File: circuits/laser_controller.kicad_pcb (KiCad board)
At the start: 4 copper layers, 173 x 61.1 mm, 180 parts, among them J1 USB_MINI_B, J2 USB_MINI_B, J5 24V DC IN, J6 CONN_RJ45, Q1 SOT-23, Q2 SOT-23, Q3 SOT-23, Q4 SOT-23, Q5 SOT-23, Q6 SOT-23, SW1 SW_PUSH, SW2 SW_PUSH, SW3 SW_PUSH, U1 SOIC-8_3.9x4.9mm_P1.27mm, U10 QFN-28-1EP_5x5mm_P0.5mm_EP3.3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, U11 SOT-23-5, U12 TSSOP-14_4.4x5mm_P0.65mm, U13 SOT-23, U14 LQFP-64_10x10mm_P0.5mm, U15 TSOT-23-6, U16 TSOT-23-6, U2 SOIC-8_3.9x4.9mm_P1.27mm, U3 SOIC-8_3.9x4.9mm_P1.27mm, U4 SOIC-8_3.9x4.9mm_P1.27mm, U5 SOT-23-5, U6 SOT-23-5, U7 SOT-23-5, U8 SOT-23-5, U9 ESP32-S3-WROOM-1

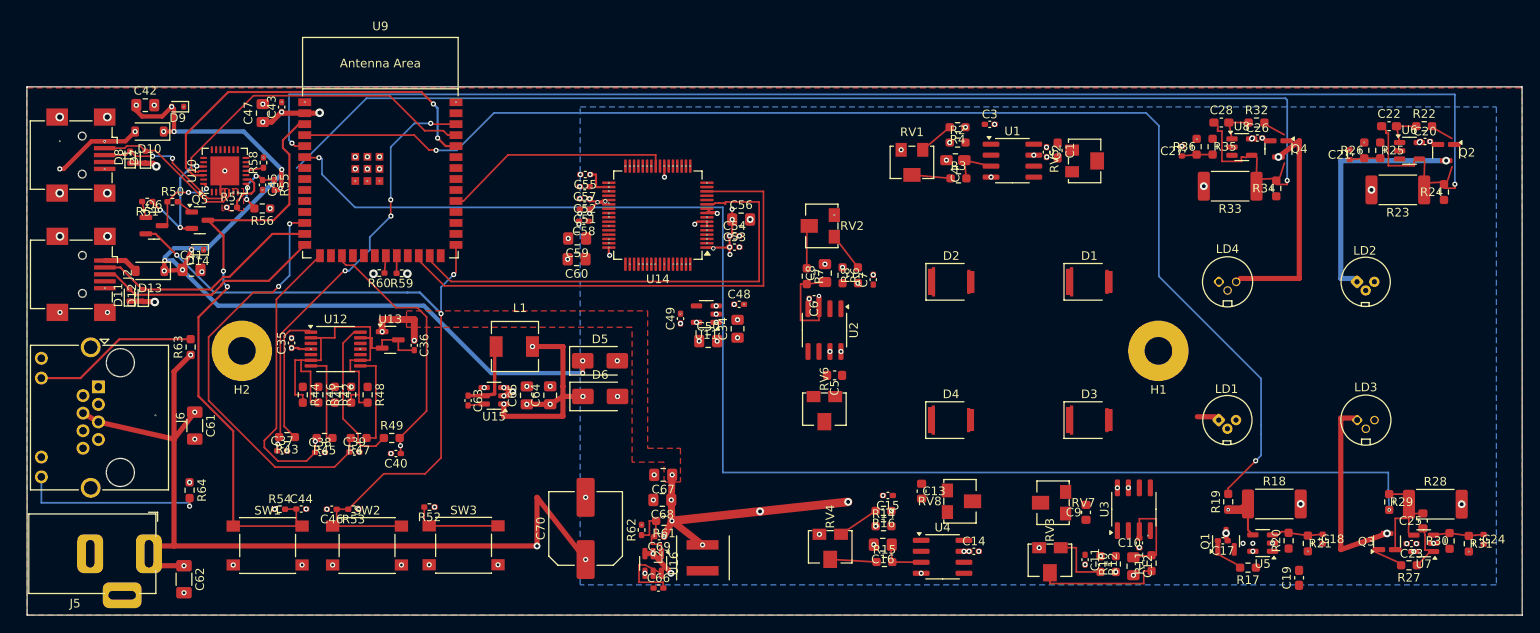
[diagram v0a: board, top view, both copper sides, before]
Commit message: fix(pcb): remove dangling trace stubs
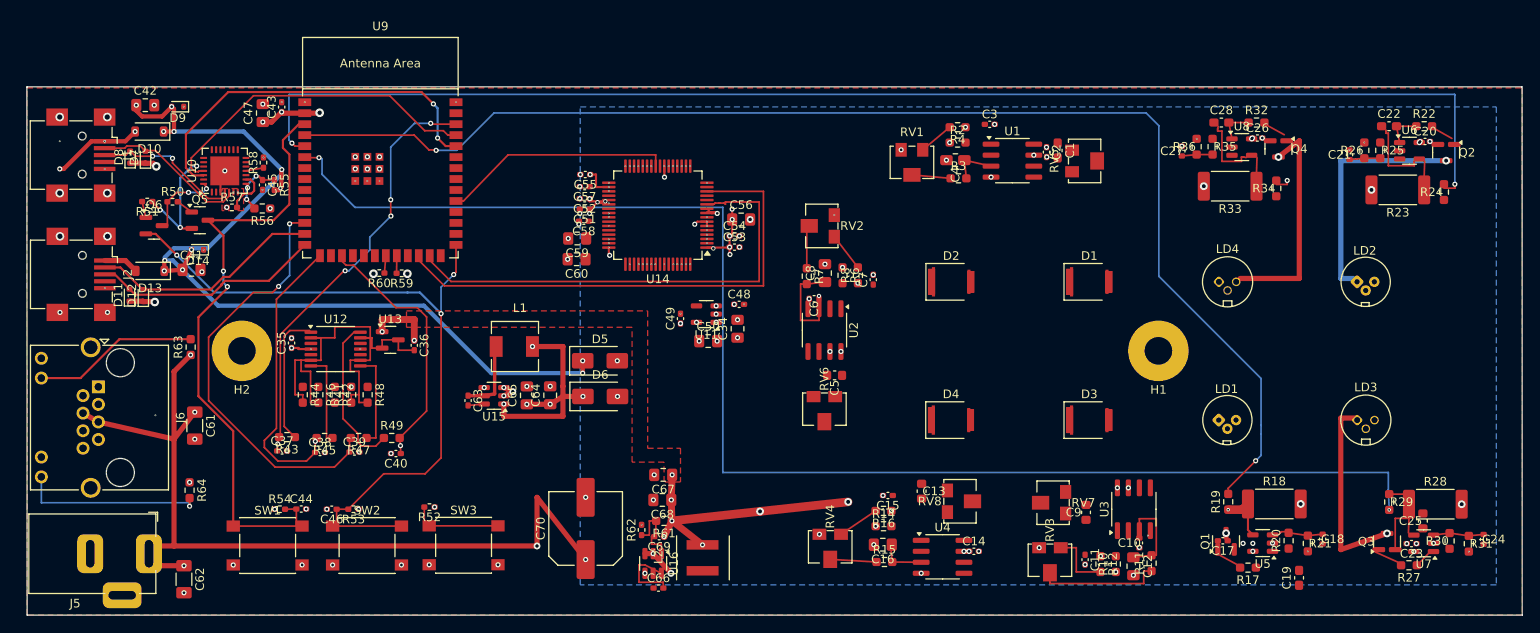
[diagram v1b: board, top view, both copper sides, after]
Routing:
- net ISENSE4: track 129.1 -> 1.72 mm
- net /LASER_BLUE/FB: track 12.4 -> 9.56 mm
- net /LASER_RED/FB: track 12.4 -> 9.59 mm
- net /LASER_GREEN/LOUT: track 3.69 -> 1.23 mm
- net LASER_N1: track 2.05 -> 0.00 mm
- net /MCU_ESP32-S3/RTS: track 15.7 -> 14.1 mm
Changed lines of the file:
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@@
   (via (at 192.0835 86.324) (size 0.6) (drill 0.3) (layers "F.Cu" "B.Cu") (net 2))
   (via (at 172.6835 85.899) (size 0.6) (drill 0.3) (layers "F.Cu" "B.Cu") (net 2))
-  (segment (start 173.91 90.5575) (end 175.101 90.4928) (width 0.2) (layer "F.Cu") (net 3))
-  (segment (start 176.478 88.692) (end 175.971 90.269) (width 0.2) (layer "F.Cu") (net 3))
   (segment (start 173.306 88.059) (end 173.25 89.74) (width 0.2) (layer "F.Cu") (net 3))
   (segment (start 172.061 88.059) (end 171.75 88) (width 0.2) (layer "F.Cu") (net 3))
@@
   (segment (start 170.047 84.009) (end 172.335 84.009) (width 0.2) (layer "F.Cu") (net 4))
   (segment (start 170.409 85.899) (end 170.047 84.009) (width 0.2) (layer "F.Cu") (net 4))
-  (segment (start 191.553 129.2628) (end 191.9975 129.2375) (width 0.2) (layer "F.Cu") (net 5))
   (segment (start 190.223 127.003) (end 188.602 127.003) (width 0.2) (layer "F.Cu") (net 5))
   (segment (start 190.888 129.8095) (end 190.827 131.4805) (width 0.2) (layer "F.Cu") (net 5))
@@
   (segment (start 189.3 129.8095) (end 189.3 133.425) (width 0.2) (layer "F.Cu") (net 5))
   (segment (start 193.102 133.9105) (end 192.255 134.7955) (width 0.2) (layer "F.Cu") (net 6))
-  (segment (start 192.6675 131.4025) (end 192.75 131.75) (width 0.2) (layer "F.Cu") (net 6))
-  (segment (start 192.75 131.75) (end 192.75 133.5) (width 0.2) (layer "F.Cu") (net 6))
-  (segment (start 192.75 133.5) (end 193.102 133.4688) (width 0.2) (layer "F.Cu") (net 6))
   (segment (start 172.261 131.151) (end 172.8275 131.7175) (width 0.25) (layer "F.Cu") (net 7))
   (segment (start 172.261 128.1415) (end 172.261 131.151) (width 0.25) (layer "F.Cu") (net 7))
@@
   (segment (start 171.6025 128.8) (end 172.261 128.1415) (width 1) (layer "F.Cu") (net 7))
   (via (at 169.975 128.8) (size 0.4) (drill 0.2) (layers "F.Cu" "B.Cu") (net 7))
-  (segment (start 194.501 90.9178) (end 193.31 90.9825) (width 0.2) (layer "F.Cu") (net 9))
-  (segment (start 195.371 90.694) (end 195.878 89.117) (width 0.2) (layer "F.Cu") (net 9))
   (segment (start 192.65 90.165) (end 192.706 88.484) (width 0.2) (layer "F.Cu") (net 9))
   (segment (start 188.219 84.869) (end 188.25 85) (width 0.2) (layer "F.Cu") (net 9))
@@
   (segment (start 80.35962 101.6) (end 78.9 103.05962) (width 0.2) (layer "B.Cu") (net 31))
   (segment (start 78.9 103.05962) (end 78.9 106.125) (width 0.2) (layer "B.Cu") (net 31))
-  (segment (start 50.678442 89.1) (end 50.625 89.046558) (width 0.25) (layer "F.Cu") (net 32))
   (segment (start 48.8375 96.2625) (end 48.725 96.15) (width 0.25) (layer "F.Cu") (net 32))
-  (segment (start 51.425 89.1) (end 50.678442 89.1) (width 0.25) (layer "F.Cu") (net 32))
   (segment (start 50.05 96.2625) (end 48.8375 96.2625) (width 0.25) (layer "F.Cu") (net 32))
   (segment (start 45.5 93.15) (end 45.5 93.225) (width 0.25) (layer "F.Cu") (net 32))
@@
   (via (at 48.725 96.15) (size 0.6) (drill 0.3) (layers "F.Cu" "B.Cu") (net 32))
   (segment (start 48.725 90.4) (end 50.078442 89.046558) (width 0.25) (layer "B.Cu") (net 32))
-  (segment (start 51.425 89.1) (end 50.678442 89.1) (width 0.25) (layer "B.Cu") (net 32))
-  (segment (start 50.678442 89.1) (end 50.625 89.046558) (width 0.25) (layer "B.Cu") (net 32))
   (segment (start 48.625 96.15) (end 48.725 96.15) (width 0.25) (layer "B.Cu") (net 32))
   (segment (start 46.6 94.125) (end 48.625 96.15) (width 0.25) (layer "B.Cu") (net 32))
@@
   (segment (start 176.8 91.17) (end 175.536 91.17) (width 0.2) (layer "F.Cu") (net 50))
   (via (at 176.8 90.7165) (size 0.6) (drill 0.3) (layers "F.Cu" "B.Cu") (net 50))
-  (segment (start 70.27318 81.20182) (end 176.60182 81.20182) (width 0.2) (layer "B.Cu") (net 50))
-  (segment (start 62.2 89.275) (end 70.27318 81.20182) (width 0.2) (layer "B.Cu") (net 50))
-  (segment (start 176.8 81.4) (end 176.8 90.7165) (width 0.2) (layer "B.Cu") (net 50))
-  (segment (start 176.60182 81.20182) (end 176.8 81.4) (width 0.2) (layer "B.Cu") (net 50))
-  (segment (start 168.45 118.05) (end 166.4 118.05) (width 0.6) (layer "F.Cu") (net 51))
   (via (at 169.723 131.522) (size 0.9) (drill 0.45) (layers "F.Cu" "B.Cu") (net 51))
   (via (at 195.188 88.4195) (size 0.9) (drill 0.45) (layers "F.Cu" "B.Cu") (net 52))

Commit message: chore(pcb): checkpoint current layout before power plane cleanup
Rotate backup snapshots ahead of restructuring power planes into
standard 24V/GND/3V3/5V regions and de-overlapping PD/laser components.
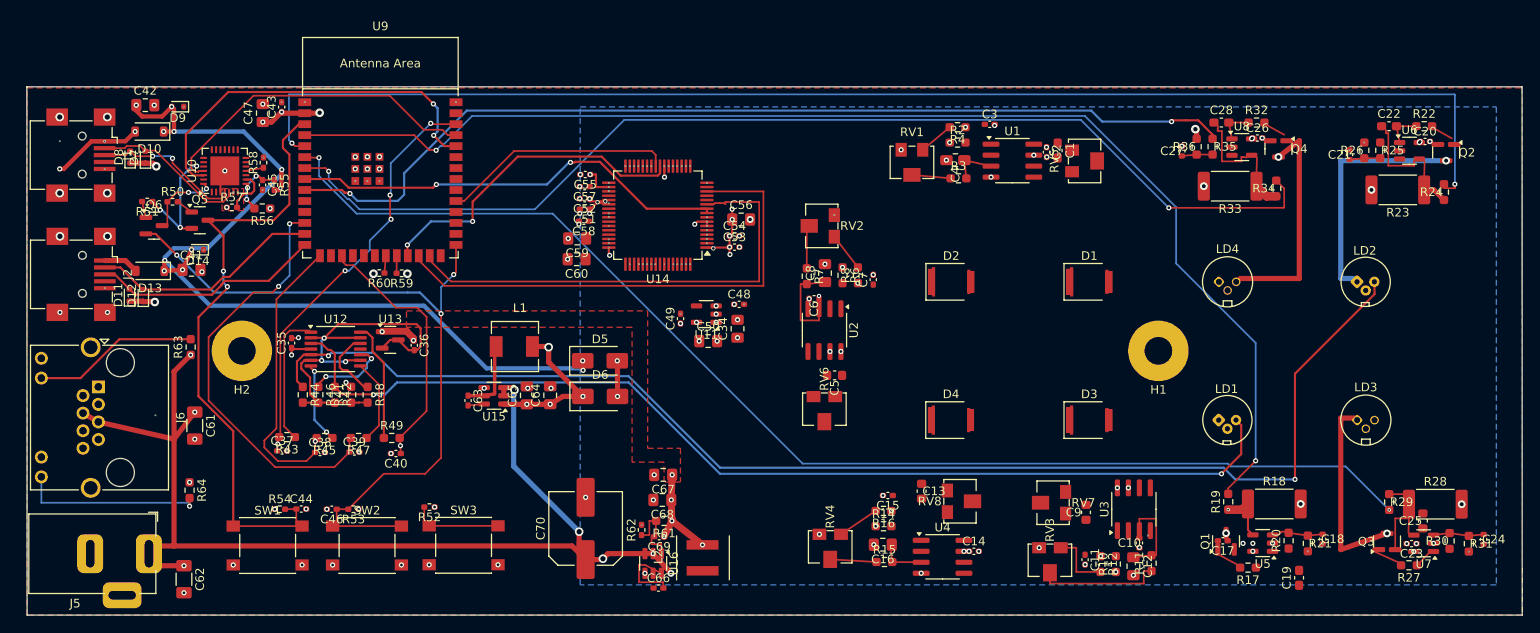
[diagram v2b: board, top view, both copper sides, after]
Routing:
- net MPD_RAW2: track 0.00 -> 152.0 mm, vias 0 -> 2
- net ISENSE4: track 1.72 -> 127.9 mm, vias 1 -> 2
- net MPD_RAW1: track 0.00 -> 122.4 mm, vias 0 -> 2
- net PWM4: track 0.00 -> 113.2 mm, vias 0 -> 2
- net CONVST: track 2.69 -> 50.9 mm, vias 1 -> 2
- net ADC_MISO_A: track 0.00 -> 37.9 mm, vias 0 -> 2
- net LASER_V+: track 39.9 -> 16.1 mm, vias 9 -> 7
- net VIN_24V: track 109.3 -> 131.1 mm, vias 10 -> 8
- net ISENSE3: track 163.8 -> 143.6 mm
- net MPD_RAW3: track 0.00 -> 9.46 mm, vias 0 -> 2
- net MPD_RAW4: track 0.00 -> 8.38 mm
- net /POWER_IO/BUCK_5V: track 26.6 -> 18.7 mm, vias 5 -> 4
- net ISENSE1: track 151.0 -> 145.9 mm
- net /POWER_IO/MPD_BIAS: track 53.2 -> 48.4 mm, vias 0 -> 3
- net /POWER_IO/MPD_AMP4: track 18.3 -> 13.8 mm
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
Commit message: fix(pcb): eliminate all 25 component courtyard overlaps
Zero footprint-body overlaps and zero different-net pad overlaps now,
verified against a fresh courtyard-polygon analysis (not just pad
bboxes). Worst offender was J6 (RJ45) grossly overlapping the whole
J2/D11/D12/D13 USB cluster (10.75x6.23mm); the rest were per-channel
TIA/laser-driver decoupling caps squeezed against their op-amp/FET by
the HandSolder footprint variants being larger than the original
template spacing assumed.

Verified against the project's own PLACEMENT_CHECKS: identical 71/111
pass/fail set before and after -- these moves introduced zero new
placement-distance violations and fixed zero pre-existing ones (those
71 predate this change, from the board's hand-placement/resize, and
are a separate concern from overlap cleanup).
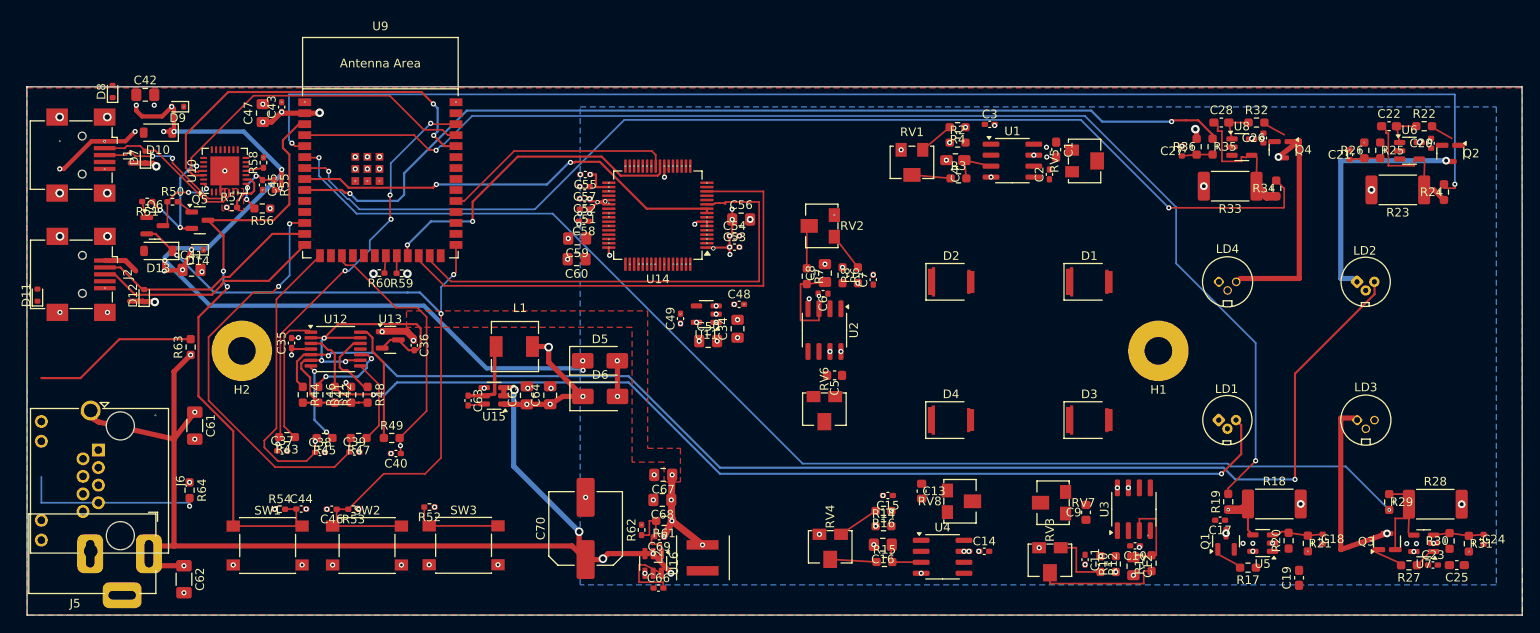
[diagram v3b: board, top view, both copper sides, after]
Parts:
- moved D11 10.6 mm to (32.2, 104.0)
- moved D8 7.85 mm to (40.9, 80.4)
- moved J6 7.31 mm to (39.2, 121.9)
- moved C25 6.45 mm to (196.4, 135.2), turned to 180 degrees
- moved C23 3.50 mm to (193.7, 135.2), turned to 0 degrees
- moved C2 2.60 mm to (149.3, 90.0), turned to 90 degrees
- moved D13 2.50 mm to (46.2, 98.9)
- moved C17 2.40 mm to (169.0, 130.0)
- moved C6 1.20 mm to (123.1, 103.8)
- moved C42 1.20 mm to (44.7, 80.8)
- moved C14 1.20 mm to (141.8, 133.6)
- moved D10 1.00 mm to (46.1, 85.2)
- moved C20 0.72 mm to (193.4, 86.4), turned to 90 degrees
- moved C26 0.70 mm to (174.0, 85.8), turned to 90 degrees
- moved C10 0.60 mm to (159.2, 133.0), turned to 180 degrees
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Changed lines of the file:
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@@
   )
   (footprint "C_0402_1005Metric_Pad0.74x0.62mm_HandSolder" (layer "F.Cu")
-    (at 173.35 85.8)
+    (at 174.046 85.800 90)
     (descr "Capacitor SMD 0402 (1005 Metric), square (rectangular) end terminal, IPC_7351 nominal with elongated pad for handsoldering. (Body size source: IPC-SM-782 page 76, https://www.pcb-3d.com/wordpress/wp-content/uploads/ipc-sm-782a_amendment_1_and_2.pdf), generated with kicad-footprint-generator")
     (tags "capacitor handsolder")
@@
   )
   (footprint "C_0402_1005Metric_Pad0.74x0.62mm_HandSolder" (layer "F.Cu")
-    (at 191.187 132.728 180)
+    (at 193.662 135.203)
     (descr "Capacitor SMD 0402 (1005 Metric), square (rectangular) end terminal, IPC_7351 nominal with elongated pad for handsoldering. (Body size source: IPC-SM-782 page 76, https://www.pcb-3d.com/wordpress/wp-content/uploads/ipc-sm-782a_amendment_1_and_2.pdf), generated with kicad-footprint-generator")
     (tags "capacitor handsolder")
@@
   )
   (footprint "D_SOD-123" (layer "F.Cu")
-    (at 45.15 85.05 180)
+    (at 46.141 85.181 180)
     (descr "SOD-123")
     (tags "SOD-123")
@@
   )
   (footprint "D_SOD-523" (layer "F.Cu")
-    (at 44.45 104.025 90)
+    (at 44.550 104.025 90)
     (descr "http://www.diodes.com/datasheets/ap02001.pdf p.144")
     (tags "Diode SOD523")
@@
   )
   (footprint "D_SOD-523" (layer "F.Cu")
-    (at 42.925 88 90)
+    (at 40.893 80.417 90)
     (descr "http://www.diodes.com/datasheets/ap02001.pdf p.144")
     (tags "Diode SOD523")
@@
   )
   (footprint "C_0402_1005Metric_Pad0.74x0.62mm_HandSolder" (layer "F.Cu")
-    (at 169.35 132.4 180)
+    (at 169.037 130.021 180)
     (descr "Capacitor SMD 0402 (1005 Metric), square (rectangular) end terminal, IPC_7351 nominal with elongated pad for handsoldering. (Body size source: IPC-SM-782 page 76, https://www.pcb-3d.com/wordpress/wp-content/uploads/ipc-sm-782a_amendment_1_and_2.pdf), generated with kicad-footprint-generator")
     (tags "capacitor handsolder")
@@
   )
   (footprint "SOT-23" (layer "F.Cu")
-    (at 45.68 95.9375)
+    (at 45.780 95.938)
     (descr "SOT, 3 Pin (https://www.jedec.org/system/files/docs/to-236h.pdf variant AB), generated with kicad-footprint-generator ipc_gullwing_generator.py")
     (tags "SOT TO_SOT_SMD")
@@
   )
   (footprint "C_0402_1005Metric_Pad0.74x0.62mm_HandSolder" (layer "F.Cu")
-    (at 122.0575 104.4 180)
+    (at 123.097 103.800 180)
     (descr "Capacitor SMD 0402 (1005 Metric), square (rectangular) end terminal, IPC_7351 nominal with elongated pad for handsoldering. (Body size source: IPC-SM-782 page 76, https://www.pcb-3d.com/wordpress/wp-content/uploads/ipc-sm-782a_amendment_1_and_2.pdf), generated with kicad-footprint-generator")
     (tags "capacitor handsolder")
@@
   )
   (footprint "SOT-23" (layer "F.Cu")
-    (at 175.788 87.057 -90)
+    (at 176.275 87.156 270)
     (descr "SOT, 3 Pin (https://www.jedec.org/system/files/docs/to-236h.pdf variant AB), generated with kicad-footprint-generator ipc_gullwing_generator.py")
     (tags "SOT TO_SOT_SMD")
@@
   )
   (footprint "C_0603_1608Metric_Pad1.08x0.95mm_HandSolder" (layer "F.Cu")
-    (at 150.243 87.2435 -90)
+    (at 150.070 87.144 270)
     (descr "Capacitor SMD 0603 (1608 Metric), square (rectangular) end terminal, IPC_7351 nominal with elongated pad for handsoldering. (Body size source: IPC-SM-782 page 76, https://www.pcb-3d.com/wordpress/wp-content/uploads/ipc-sm-782a_amendment_1_and_2.pdf), generated with kicad-footprint-generator")
     (tags "capacitor handsolder")
@@
   )
   (footprint "C_0402_1005Metric_Pad0.74x0.62mm_HandSolder" (layer "F.Cu")
-    (at 159.695 132.65 90)
+    (at 159.198 132.986 180)
     (descr "Capacitor SMD 0402 (1005 Metric), square (rectangular) end terminal, IPC_7351 nominal with elongated pad for handsoldering. (Body size source: IPC-SM-782 page 76, https://www.pcb-3d.com/wordpress/wp-content/uploads/ipc-sm-782a_amendment_1_and_2.pdf), generated with kicad-footprint-generator")
     (tags "capacitor handsolder")
@@
   )
   (footprint "C_0603_1608Metric_Pad1.08x0.95mm_HandSolder" (layer "F.Cu")
-    (at 192.5 130.1 90)
+    (at 196.427 135.217 180)
     (descr "Capacitor SMD 0603 (1608 Metric), square (rectangular) end terminal, IPC_7351 nominal with elongated pad for handsoldering. (Body size source: IPC-SM-782 page 76, https://www.pcb-3d.com/wordpress/wp-content/uploads/ipc-sm-782a_amendment_1_and_2.pdf), generated with kicad-footprint-generator")
     (tags "capacitor handsolder")
@@
   )
   (footprint "C_0402_1005Metric_Pad0.74x0.62mm_HandSolder" (layer "F.Cu")
-    (at 140.55 133.62)
+    (at 141.750 133.620)
     (descr "Capacitor SMD 0402 (1005 Metric), square (rectangular) end terminal, IPC_7351 nominal with elongated pad for handsoldering. (Body size source: IPC-SM-782 page 76, https://www.pcb-3d.com/wordpress/wp-content/uploads/ipc-sm-782a_amendment_1_and_2.pdf), generated with kicad-footprint-generator")
     (tags "capacitor handsolder")
@@
   )
   (footprint "D_SOD-123" (layer "F.Cu")
-    (at 45.225 101.175 180)
+    (at 46.182 98.865 180)
     (descr "SOD-123")
     (tags "SOD-123")
@@
   )
   (footprint "C_0402_1005Metric_Pad0.74x0.62mm_HandSolder" (layer "F.Cu")
-    (at 148.95 87.4325 -90)
+    (at 149.289 90.010 90)
     (descr "Capacitor SMD 0402 (1005 Metric), square (rectangular) end terminal, IPC_7351 nominal with elongated pad for handsoldering. (Body size source: IPC-SM-782 page 76, https://www.pcb-3d.com/wordpress/wp-content/uploads/ipc-sm-782a_amendment_1_and_2.pdf), generated with kicad-footprint-generator")
     (tags "capacitor handsolder")
@@
   )
   (footprint "D_SOD-523" (layer "F.Cu")
-    (at 42.85 103.975 90)
+    (at 32.200 103.975 90)
     (descr "http://www.diodes.com/datasheets/ap02001.pdf p.144")
     (tags "Diode SOD523")
@@
   )
   (footprint "SOT-23" (layer "F.Cu")
-    (at 195.188 87.482 -90)
+    (at 195.675 87.581 270)
     (descr "SOT, 3 Pin (https://www.jedec.org/system/files/docs/to-236h.pdf variant AB), generated with kicad-footprint-generator ipc_gullwing_generator.py")
     (tags "SOT TO_SOT_SMD")
@@
   )
   (footprint "C_0805_2012Metric_Pad1.18x1.45mm_HandSolder" (layer "F.Cu")
-    (at 44.675 82)
+    (at 44.675 80.800)
     (descr "Capacitor SMD 0805 (2012 Metric), square (rectangular) end terminal, IPC_7351 nominal with elongated pad for handsoldering. (Body size source: IPC-SM-782 page 76, https://www.pcb-3d.com/wordpress/wp-content/uploads/ipc-sm-782a_amendment_1_and_2.pdf, https://docs.google.com/spreadsheets/d/1BsfQQcO9C6DZCsRaXUlFlo91Tg2WpOkGARC1WS5S8t0/edit?usp=sharing), generated with kicad-footprint-generator")
     (tags "capacitor handsolder")
@@
   )
   (footprint "C_0402_1005Metric_Pad0.74x0.62mm_HandSolder" (layer "F.Cu")
-    (at 192.75 86.2)
+    (at 193.446 86.400 90)
     (descr "Capacitor SMD 0402 (1005 Metric), square (rectangular) end terminal, IPC_7351 nominal with elongated pad for handsoldering. (Body size source: IPC-SM-782 page 76, https://www.pcb-3d.com/wordpress/wp-content/uploads/ipc-sm-782a_amendment_1_and_2.pdf), generated with kicad-footprint-generator")
     (tags "capacitor handsolder")
@@
   )
   (footprint "RJ45_Amphenol_RJHSE538X" (layer "F.Cu")
-    (at 39.25 114.586 -90)
+    (at 39.250 121.900 270)
     (descr "Shielded, 2 LED, https://www.amphenolcanada.com/ProductSearch/drawings/AC/RJHSE538X.pdf")
     (tags "RJ45 8p8c ethernet cat5")
